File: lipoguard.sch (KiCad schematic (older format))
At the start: 13 parts, among them P1 CONN_2, P2 CONN_2, U1 BTS6143, U2 LM358

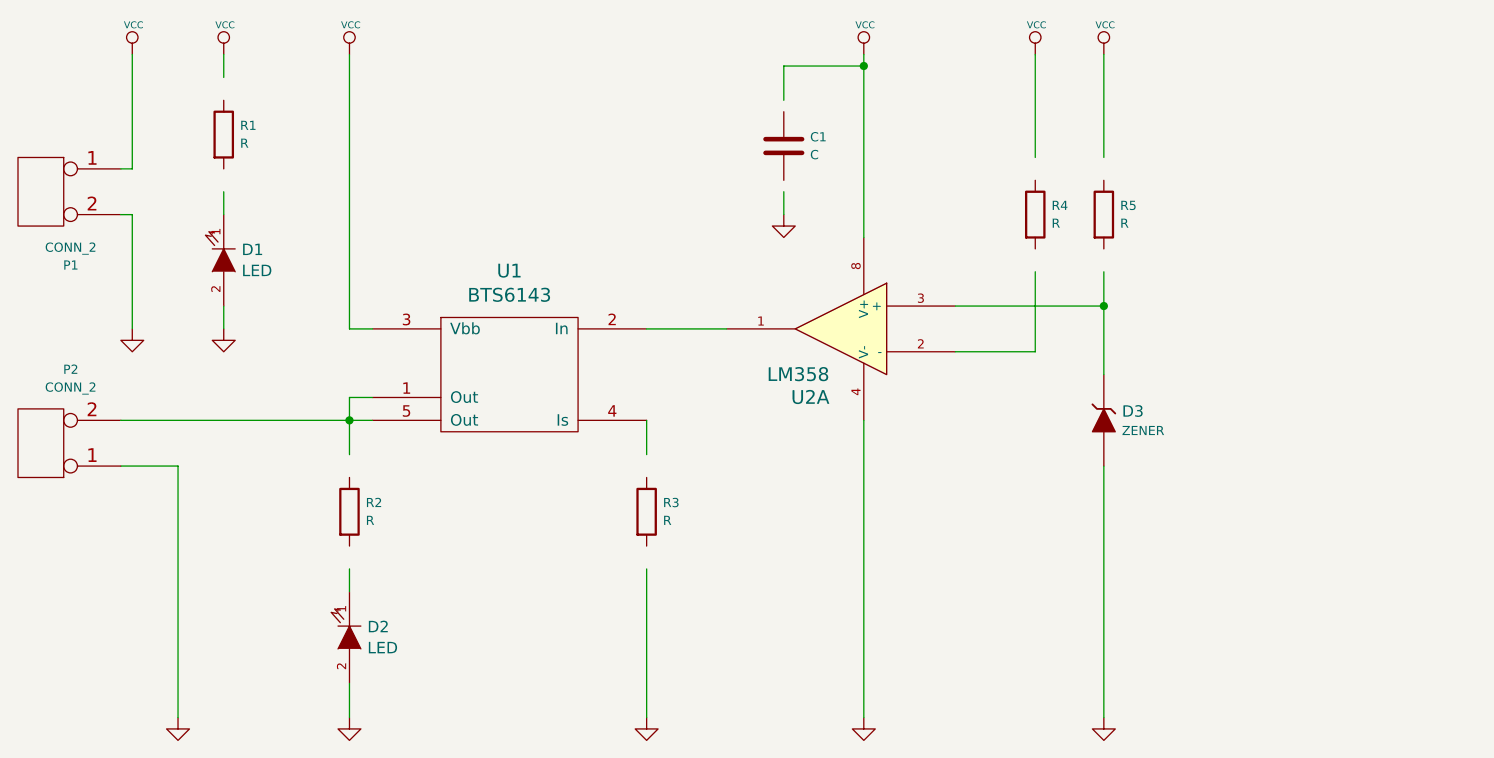
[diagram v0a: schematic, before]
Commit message: Simplified schematic
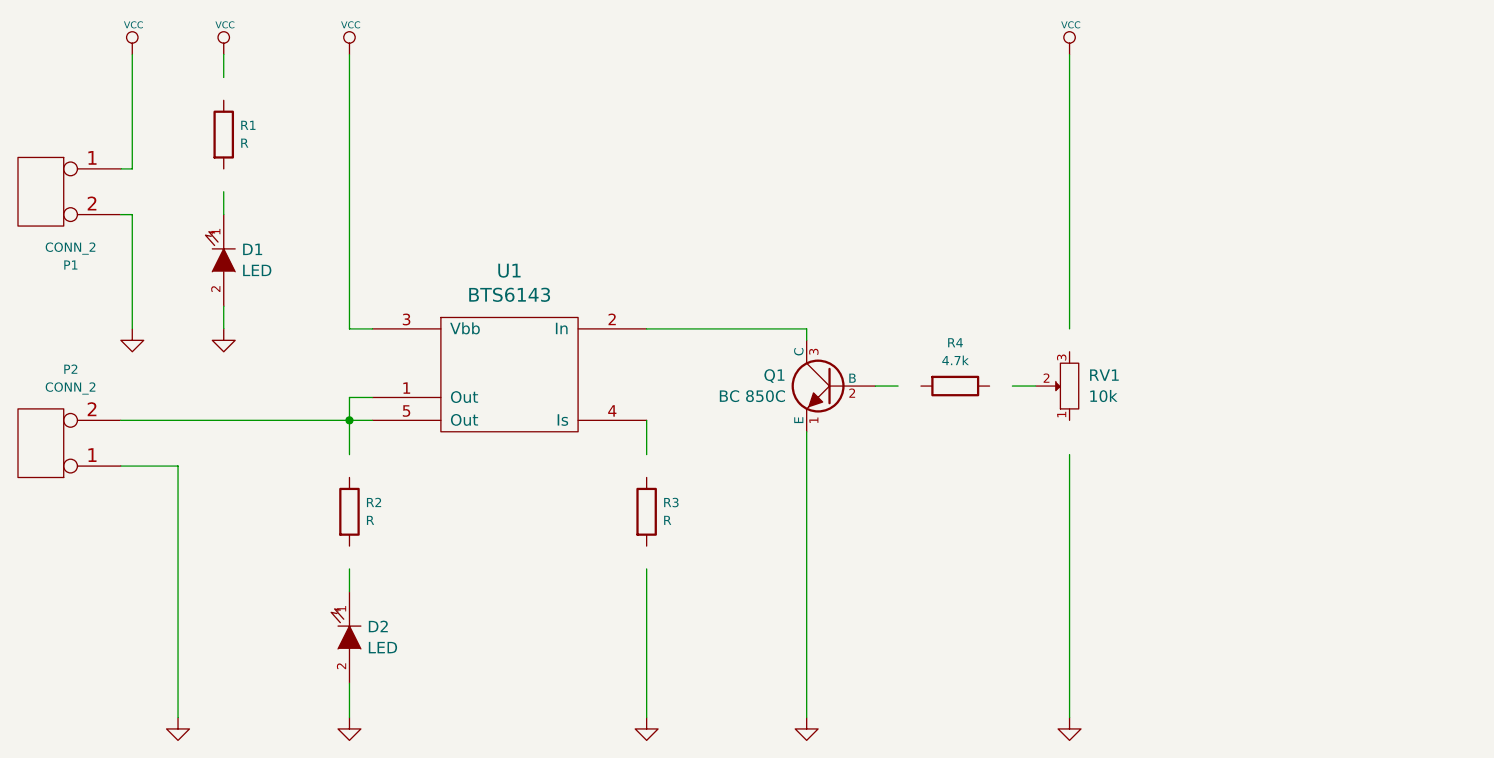
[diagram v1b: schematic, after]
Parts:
- removed C1: C, libcms:SM0603, symbol C
- removed D3: ZENER, discret:D3, symbol ZENER
- removed R5: R, libcms:SM0603, symbol R
- removed U2: LM358, smd_dil:so-8, symbol LM358
- added Q1: BC 850C, symbol NPN
- added RV1: 10k, symbol POT
- R4: value R -> 4.7k; footprint libcms:SM0603 -> (none)
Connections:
- wire segments 31 -> 25
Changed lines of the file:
@@
 $EndComp
 $Comp
-L LM358 U2
-U 1 1 57E2D977
-P 6750 3650
-F 0 "U2" H 6800 3350 60  0000 L CNN
-F 1 "LM358" H 6800 3450 60  0000 L CNN
-F 2 "smd_dil:so-8" H 6750 3650 60  0001 C CNN
-F 3 "" H 6750 3650 60  0000 C CNN
-	1    6750 3650
-	-1   0    0    -1
-$EndComp
-Wire Wire Line
-	5900 3650 6250 3650
-$Comp
-L R R5
-U 1 1 57E2DB51
-P 7900 3150
-F 0 "R5" H 7971 3189 40  0000 L CNN
-F 1 "R" H 7971 3111 40  0000 L CNN
-F 2 "libcms:SM0603" V 7830 3150 30  0001 C CNN
-F 3 "" H 7900 3150 30  0000 C CNN
-	1    7900 3150
-	1    0    0    -1
-$EndComp
-$Comp
-L VCC #PWR01
-U 1 1 57E2DBDA
-P 7900 2450
-F 0 "#PWR01" H 7900 2550 30  0001 C CNN
-F 1 "VCC" H 7906 2579 30  0000 C CNN
-F 2 "" H 7900 2450 60  0000 C CNN
-F 3 "" H 7900 2450 60  0000 C CNN
-	1    7900 2450
-	1    0    0    -1
-$EndComp
-Wire Wire Line
-	7900 2900 7900 2450
-Wire Wire Line
-	7250 3550 7900 3550
-Wire Wire Line
-	7900 3400 7900 3850
-Connection ~ 7900 3550
-$Comp
-L ZENER D3
-U 1 1 57E2DC4A
-P 7900 4050
-F 0 "D3" V 7939 3971 50  0000 R CNN
-F 1 "ZENER" V 7854 3971 40  0000 R CNN
-F 2 "discret:D3" H 7900 4050 60  0001 C CNN
-F 3 "" H 7900 4050 60  0000 C CNN
-	1    7900 4050
-	0    -1   -1   0
-$EndComp
-$Comp
-L GND #PWR02
-U 1 1 57E2DD75
-P 7900 5350
-F 0 "#PWR02" H 7900 5350 30  0001 C CNN
-F 1 "GND" H 7900 5280 30  0001 C CNN
-F 2 "" H 7900 5350 60  0000 C CNN
-F 3 "" H 7900 5350 60  0000 C CNN
-	1    7900 5350
-	1    0    0    -1
-$EndComp
-Wire Wire Line
-	7900 4250 7900 5350
-Wire Wire Line
-	7250 3750 7600 3750
-$Comp
-L VCC #PWR03
-U 1 1 57E2DDB7
-P 7600 2450
-F 0 "#PWR03" H 7600 2550 30  0001 C CNN
-F 1 "VCC" H 7606 2579 30  0000 C CNN
-F 2 "" H 7600 2450 60  0000 C CNN
-F 3 "" H 7600 2450 60  0000 C CNN
-	1    7600 2450
-	1    0    0    -1
-$EndComp
-$Comp
-L VCC #PWR04
-U 1 1 57E2E02D
-P 6850 2450
-F 0 "#PWR04" H 6850 2550 30  0001 C CNN
-F 1 "VCC" H 6856 2579 30  0000 C CNN
-F 2 "" H 6850 2450 60  0000 C CNN
-F 3 "" H 6850 2450 60  0000 C CNN
-	1    6850 2450
-	1    0    0    -1
-$EndComp
-Wire Wire Line
-	6850 2450 6850 3250
-Wire Wire Line
-	6850 4050 6850 5350
-$Comp
-L GND #PWR05
-U 1 1 57E2E078
-P 6850 5350
-F 0 "#PWR05" H 6850 5350 30  0001 C CNN
-F 1 "GND" H 6850 5280 30  0001 C CNN
-F 2 "" H 6850 5350 60  0000 C CNN
-F 3 "" H 6850 5350 60  0000 C CNN
-	1    6850 5350
-	1    0    0    -1
-$EndComp
-$Comp
-L GND #PWR06
+L GND #PWR01
 U 1 1 57E2E094
 P 5900 5350
-F 0 "#PWR06" H 5900 5350 30  0001 C CNN
+F 0 "#PWR01" H 5900 5350 30  0001 C CNN
 F 1 "GND" H 5900 5280 30  0001 C CNN
 F 2 "" H 5900 5350 60  0000 C CNN
@@
 	4600 3650 4600 2450
 $Comp
-L VCC #PWR07
+L VCC #PWR02
 U 1 1 57E2E14D
 P 4600 2450
-F 0 "#PWR07" H 4600 2550 30  0001 C CNN
+F 0 "#PWR02" H 4600 2550 30  0001 C CNN
 F 1 "VCC" H 4606 2579 30  0000 C CNN
 F 2 "" H 4600 2450 60  0000 C CNN
@@
 	1    0    0    -1
 $EndComp
-$Comp
-L R R4
-U 1 1 57E2E21E
-P 7600 3150
-F 0 "R4" H 7671 3189 40  0000 L CNN
-F 1 "R" H 7671 3111 40  0000 L CNN
-F 2 "libcms:SM0603" V 7530 3150 30  0001 C CNN
-F 3 "" H 7600 3150 30  0000 C CNN
-	1    7600 3150
-	1    0    0    -1
-$EndComp
-Wire Wire Line
-	7600 2900 7600 2450
-Wire Wire Line
-	7600 3750 7600 3400
 $Comp
 L CONN_2 P2
@@
 	3850 4250 3850 5350
 $Comp
-L GND #PWR08
+L GND #PWR03
 U 1 1 57E2E353
 P 3850 5350
-F 0 "#PWR08" H 3850 5350 30  0001 C CNN
+F 0 "#PWR03" H 3850 5350 30  0001 C CNN
 F 1 "GND" H 3850 5280 30  0001 C CNN
 F 2 "" H 3850 5350 60  0000 C CNN
@@
 	4600 4700 4600 4800
 $Comp
-L GND #PWR09
+L GND #PWR04
 U 1 1 57E2E82E
 P 4600 5350
-F 0 "#PWR09" H 4600 5350 30  0001 C CNN
+F 0 "#PWR04" H 4600 5350 30  0001 C CNN
 F 1 "GND" H 4600 5280 30  0001 C CNN
 F 2 "" H 4600 5350 60  0000 C CNN
@@
 	4600 5350 4600 5200
 $Comp
-L C C1
-U 1 1 57E2ECEA
-P 6500 2850
-F 0 "C1" H 6615 2889 40  0000 L CNN
-F 1 "C" H 6615 2811 40  0000 L CNN
-F 2 "libcms:SM0603" H 6538 2700 30  0001 C CNN
-F 3 "" H 6500 2850 60  0000 C CNN
-	1    6500 2850
-	1    0    0    -1
-$EndComp
-$Comp
-L GND #PWR010
-U 1 1 57E2ED94
-P 6500 3150
-F 0 "#PWR010" H 6500 3150 30  0001 C CNN
-F 1 "GND" H 6500 3080 30  0001 C CNN
-F 2 "" H 6500 3150 60  0000 C CNN
-F 3 "" H 6500 3150 60  0000 C CNN
-	1    6500 3150
-	1    0    0    -1
-$EndComp
-Wire Wire Line
-	6500 3150 6500 3050
-Wire Wire Line
-	6500 2650 6500 2500
-Wire Wire Line
-	6500 2500 6850 2500
-Connection ~ 6850 2500
-$Comp
-L VCC #PWR011
+L VCC #PWR05
 U 1 1 57E2F4D3
 P 4050 2450
-F 0 "#PWR011" H 4050 2550 30  0001 C CNN
+F 0 "#PWR05" H 4050 2550 30  0001 C CNN
 F 1 "VCC" H 4056 2579 30  0000 C CNN
 F 2 "" H 4050 2450 60  0000 C CNN
@@
 $EndComp
 $Comp
-L GND #PWR012
+L GND #PWR06
 U 1 1 57E2FB8C
 P 4050 3650
-F 0 "#PWR012" H 4050 3650 30  0001 C CNN
+F 0 "#PWR06" H 4050 3650 30  0001 C CNN
 F 1 "GND" H 4050 3580 30  0001 C CNN
 F 2 "" H 4050 3650 60  0000 C CNN
@@
 	3650 3150 3650 3650
 $Comp
-L GND #PWR013
+L GND #PWR07
 U 1 1 57E30655
 P 3650 3650
-F 0 "#PWR013" H 3650 3650 30  0001 C CNN
+F 0 "#PWR07" H 3650 3650 30  0001 C CNN
 F 1 "GND" H 3650 3580 30  0001 C CNN
 F 2 "" H 3650 3650 60  0000 C CNN
@@
 $EndComp
 $Comp
-L VCC #PWR014
+L VCC #PWR08
 U 1 1 57E30683
 P 3650 2450
-F 0 "#PWR014" H 3650 2550 30  0001 C CNN
+F 0 "#PWR08" H 3650 2550 30  0001 C CNN
 F 1 "VCC" H 3656 2579 30  0000 C CNN
 F 2 "" H 3650 2450 60  0000 C CNN
@@
 	1    0    0    -1
 $EndComp
+$Comp
+L NPN Q1
+U 1 1 57F2671F
+P 6700 3900
+F 0 "Q1" H 6891 3946 50  0000 L CNN
+F 1 "BC 850C" H 6891 3854 50  0000 L CNN
+F 2 "" H 6700 3900 60  0000 C CNN
+F 3 "" H 6700 3900 60  0000 C CNN
+	1    6700 3900
+	-1   0    0    -1
+$EndComp
+Wire Wire Line
+	6600 3650 6600 3700
+Wire Wire Line
+	5900 3650 6600 3650
+Wire Wire Line
+	6600 4100 6600 5350
+$Comp
+L GND #PWR09
+U 1 1 57F26963
+P 6600 5350
+F 0 "#PWR09" H 6600 5350 30  0001 C CNN
+F 1 "GND" H 6600 5280 30  0001 C CNN
+F 2 "" H 6600 5350 60  0000 C CNN
+F 3 "" H 6600 5350 60  0000 C CNN
+	1    6600 5350
+	1    0    0    -1
+$EndComp
+$Comp
+L R R4
+U 1 1 57F269B7
+P 7250 3900
+F 0 "R4" V 7062 3900 40  0000 C CNN
+F 1 "4.7k" V 7140 3900 40  0000 C CNN
+F 2 "" V 7180 3900 30  0000 C CNN
+F 3 "" H 7250 3900 30  0000 C CNN
+	1    7250 3900
+	0    1    1    0
+$EndComp
+Wire Wire Line
+	6900 3900 7000 3900
+$Comp
+L POT RV1
+U 1 1 57F26A5C
+P 7750 3900
+F 0 "RV1" V 7796 3817 50  0000 R CNN
+F 1 "10k" V 7704 3817 50  0000 R CNN
+F 2 "" H 7750 3900 60  0000 C CNN
+F 3 "" H 7750 3900 60  0000 C CNN
+	1    7750 3900
+	0    -1   -1   0
+$EndComp
+Wire Wire Line
+	7500 3900 7600 3900
+Wire Wire Line
+	7750 4200 7750 5350
+$Comp
+L GND #PWR010
+U 1 1 57F26B56
+P 7750 5350
+F 0 "#PWR010" H 7750 5350 30  0001 C CNN
+F 1 "GND" H 7750 5280 30  0001 C CNN
+F 2 "" H 7750 5350 60  0000 C CNN
+F 3 "" H 7750 5350 60  0000 C CNN
+	1    7750 5350
+	1    0    0    -1
+$EndComp
+Wire Wire Line
+	7750 3650 7750 2450
+$Comp
+L VCC #PWR011
+U 1 1 57F26BA7
+P 7750 2450
+F 0 "#PWR011" H 7750 2550 30  0001 C CNN
+F 1 "VCC" H 7756 2579 30  0000 C CNN
+F 2 "" H 7750 2450 60  0000 C CNN
+F 3 "" H 7750 2450 60  0000 C CNN
+	1    7750 2450
+	1    0    0    -1
+$EndComp

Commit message: Finished cleaning up
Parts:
- added C1: 100nf, libcms:SM0603, symbol C
- Q1: footprint (none) -> misc:sot23BEC
- R3: footprint discret:R3 -> libcms:SM0603
- R4: footprint (none) -> libcms:SM0603
- RV1: footprint (none) -> misc:trimmer1
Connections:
- wire segments 25 -> 27
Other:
- moved on the sheet: RV1
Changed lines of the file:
@@
 F 0 "R3" H 5971 4489 40  0000 L CNN
 F 1 "R" H 5971 4411 40  0000 L CNN
-F 2 "discret:R3" V 5830 4450 30  0001 C CNN
+F 2 "libcms:SM0603" V 5830 4450 30  0001 C CNN
 F 3 "" H 5900 4450 30  0000 C CNN
 	1    5900 4450
@@
 F 0 "Q1" H 6891 3946 50  0000 L CNN
 F 1 "BC 850C" H 6891 3854 50  0000 L CNN
-F 2 "" H 6700 3900 60  0000 C CNN
+F 2 "misc:sot23BEC" H 6700 3900 60  0001 C CNN
 F 3 "" H 6700 3900 60  0000 C CNN
 	1    6700 3900
@@
 F 0 "R4" V 7062 3900 40  0000 C CNN
 F 1 "4.7k" V 7140 3900 40  0000 C CNN
-F 2 "" V 7180 3900 30  0000 C CNN
+F 2 "libcms:SM0603" V 7180 3900 30  0001 C CNN
 F 3 "" H 7250 3900 30  0000 C CNN
 	1    7250 3900
@@
 L POT RV1
 U 1 1 57F26A5C
-P 7750 3900
-F 0 "RV1" V 7796 3817 50  0000 R CNN
-F 1 "10k" V 7704 3817 50  0000 R CNN
-F 2 "" H 7750 3900 60  0000 C CNN
-F 3 "" H 7750 3900 60  0000 C CNN
-	1    7750 3900
+P 8200 3900
+F 0 "RV1" V 8246 3817 50  0000 R CNN
+F 1 "10k" V 8154 3817 50  0000 R CNN
+F 2 "misc:trimmer1" H 8200 3900 60  0001 C CNN
+F 3 "" H 8200 3900 60  0000 C CNN
+	1    8200 3900
 	0    -1   -1   0
 $EndComp
 Wire Wire Line
-	7500 3900 7600 3900
-Wire Wire Line
-	7750 4200 7750 5350
+	7500 3900 8050 3900
+Wire Wire Line
+	8200 4150 8200 5350
 $Comp
 L GND #PWR010
 U 1 1 57F26B56
-P 7750 5350
-F 0 "#PWR010" H 7750 5350 30  0001 C CNN
-F 1 "GND" H 7750 5280 30  0001 C CNN
-F 2 "" H 7750 5350 60  0000 C CNN
-F 3 "" H 7750 5350 60  0000 C CNN
-	1    7750 5350
-	1    0    0    -1
-$EndComp
-Wire Wire Line
-	7750 3650 7750 2450
+P 8200 5350
+F 0 "#PWR010" H 8200 5350 30  0001 C CNN
+F 1 "GND" H 8200 5280 30  0001 C CNN
+F 2 "" H 8200 5350 60  0000 C CNN
+F 3 "" H 8200 5350 60  0000 C CNN
+	1    8200 5350
+	1    0    0    -1
+$EndComp
+Wire Wire Line
+	8200 3650 8200 2450
 $Comp
 L VCC #PWR011
 U 1 1 57F26BA7
-P 7750 2450
-F 0 "#PWR011" H 7750 2550 30  0001 C CNN
-F 1 "VCC" H 7756 2579 30  0000 C CNN
-F 2 "" H 7750 2450 60  0000 C CNN
-F 3 "" H 7750 2450 60  0000 C CNN
-	1    7750 2450
-	1    0    0    -1
-$EndComp
+P 8200 2450
+F 0 "#PWR011" H 8200 2550 30  0001 C CNN
+F 1 "VCC" H 8206 2579 30  0000 C CNN
+F 2 "" H 8200 2450 60  0000 C CNN
+F 3 "" H 8200 2450 60  0000 C CNN
+	1    8200 2450
+	1    0    0    -1
+$EndComp
+$Comp
+L C C1
+U 1 1 57F3D205
+P 7750 4450
+F 0 "C1" H 7750 4550 40  0000 L CNN
+F 1 "100nf" H 7756 4365 40  0000 L CNN
+F 2 "libcms:SM0603" H 7788 4300 30  0001 C CNN
+F 3 "" H 7750 4450 60  0000 C CNN
+	1    7750 4450
+	1    0    0    -1
+$EndComp
+Wire Wire Line
+	7750 4250 7750 3900
+Connection ~ 7750 3900
+Wire Wire Line
+	7750 4650 7750 5350
+$Comp
+L GND #PWR012
+U 1 1 57F3D38A
+P 7750 5350
+F 0 "#PWR012" H 7750 5350 30  0001 C CNN
+F 1 "GND" H 7750 5280 30  0001 C CNN
+F 2 "" H 7750 5350 60  0001 C CNN
+F 3 "" H 7750 5350 60  0001 C CNN
+	1    7750 5350
+	1    0    0    -1
+$EndComp

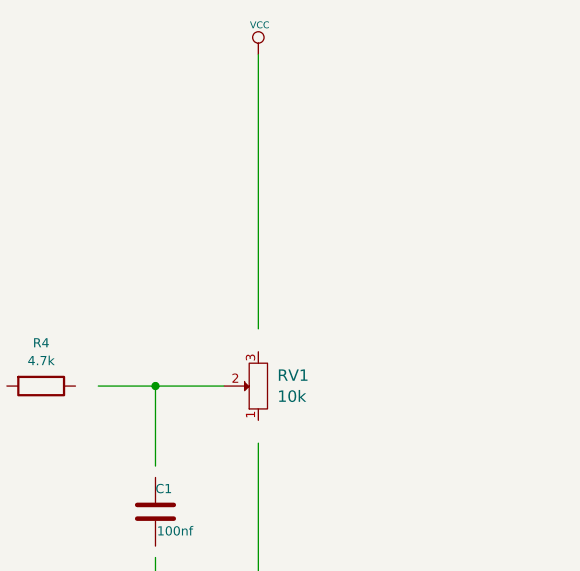
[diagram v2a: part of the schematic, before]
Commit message: Added resistor for better threshold adjustment
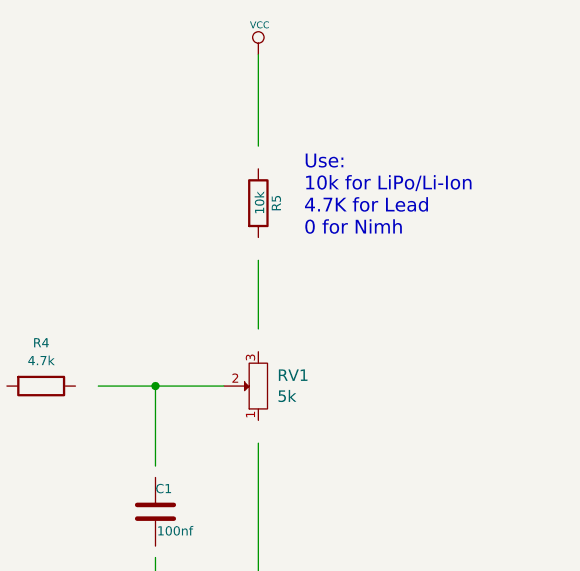
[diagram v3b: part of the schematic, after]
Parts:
- added R5: 10k, libcms:SM0603, symbol R
- RV1: value 10k -> 5k
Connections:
- wire segments 27 -> 28
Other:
- note added: "Use:\n10k for LiPo/Li-Ion\n4.7K for Lead\n0 for Nimh"
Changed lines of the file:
@@
 Wire Wire Line
 	6900 3900 7000 3900
-$Comp
-L POT RV1
-U 1 1 57F26A5C
-P 8200 3900
-F 0 "RV1" V 8246 3817 50  0000 R CNN
-F 1 "10k" V 8154 3817 50  0000 R CNN
-F 2 "misc:trimmer1" H 8200 3900 60  0001 C CNN
-F 3 "" H 8200 3900 60  0000 C CNN
-	1    8200 3900
-	0    -1   -1   0
-$EndComp
 Wire Wire Line
 	7500 3900 8050 3900
@@
 	1    0    0    -1
 $EndComp
-Wire Wire Line
-	8200 3650 8200 2450
 $Comp
 L VCC #PWR011
@@
 	1    0    0    -1
 $EndComp
+$Comp
+L POT RV1
+U 1 1 57F26A5C
+P 8200 3900
+F 0 "RV1" V 8246 3817 50  0000 R CNN
+F 1 "5k" V 8154 3817 50  0000 R CNN
+F 2 "misc:trimmer1" H 8200 3900 60  0001 C CNN
+F 3 "" H 8200 3900 60  0000 C CNN
+	1    8200 3900
+	0    -1   -1   0
+$EndComp
+$Comp
+L R R5
+U 1 1 57F56FF8
+P 8200 3100
+F 0 "R5" V 8280 3100 40  0000 C CNN
+F 1 "10k" V 8207 3101 40  0000 C CNN
+F 2 "libcms:SM0603" V 8130 3100 30  0001 C CNN
+F 3 "" H 8200 3100 30  0000 C CNN
+	1    8200 3100
+	1    0    0    -1
+$EndComp
+Wire Wire Line
+	8200 3650 8200 3350
+Wire Wire Line
+	8200 2850 8200 2450
+Text Notes 8400 3250 0    60   ~ 0
+Use:\n10k for LiPo/Li-Ion\n4.7K for Lead\n0 for Nimh
 $EndSCHEMATC
